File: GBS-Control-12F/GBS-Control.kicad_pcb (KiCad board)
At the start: 2 copper layers, 41.3 x 28.6 mm, 16 parts, among them J1 PROG, U1 PLCC-44 socket, U2 ESP-12F

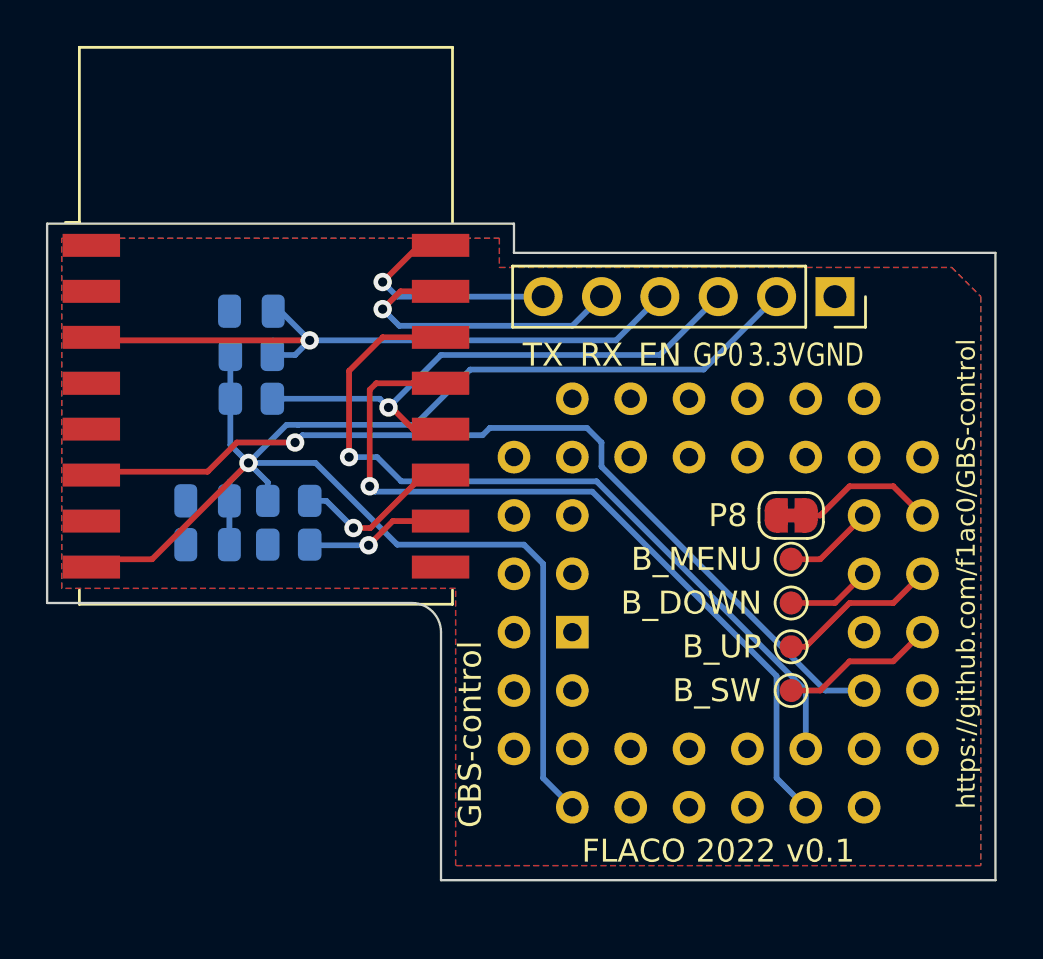
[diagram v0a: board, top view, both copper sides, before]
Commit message: KiCAD : add a port to connect the Si5351 Clock Generator
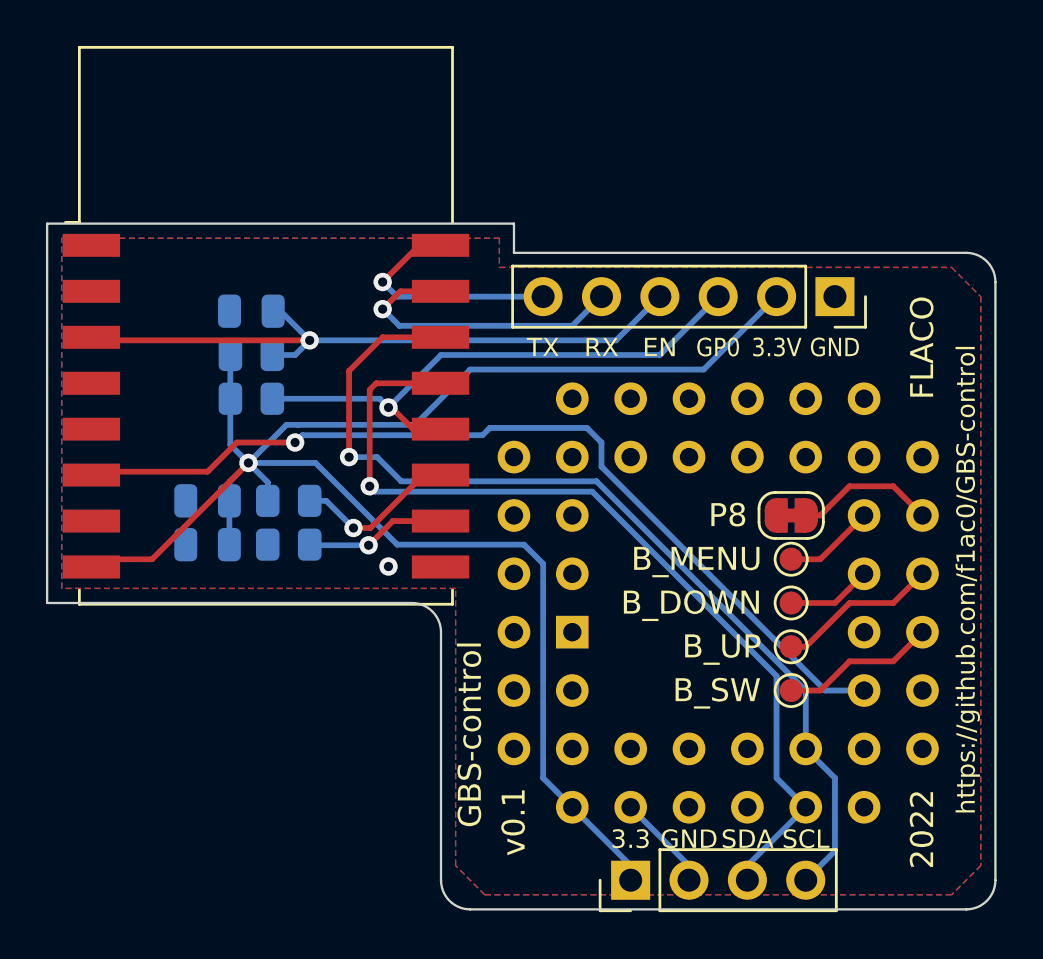
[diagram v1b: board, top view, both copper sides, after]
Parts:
- added J2: Clock port, Connector_PinHeader_2.54mm:PinHeader_1x04_P2.54mm_Vertical, F.Cu at (138.4, 102.9)
- TP1: value TestPoint -> B_UP
- TP2: value TestPoint -> B_DOWN
- TP3: value TestPoint -> B_SW
- TP4: value TestPoint -> B_MENU
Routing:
- net /SCL: track 35.0 -> 41.7 mm
- net /SDA: track 34.8 -> 39.0 mm
- net +3.3V: track 71.4 -> 75.6 mm
- net GND: track 0.00 -> 4.23 mm, vias 0 -> 1
- net /DISABLE: track 6.75 -> 6.12 mm
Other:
- board size 41.3 x 28.6 mm -> 41.3 x 29.8 mm
- board text added: "2022"
- board text added: "3.3"
- board text added: "FLACO"
- board text added: "SCL"
- board text added: "SDA"
- board text added: "v0.1"

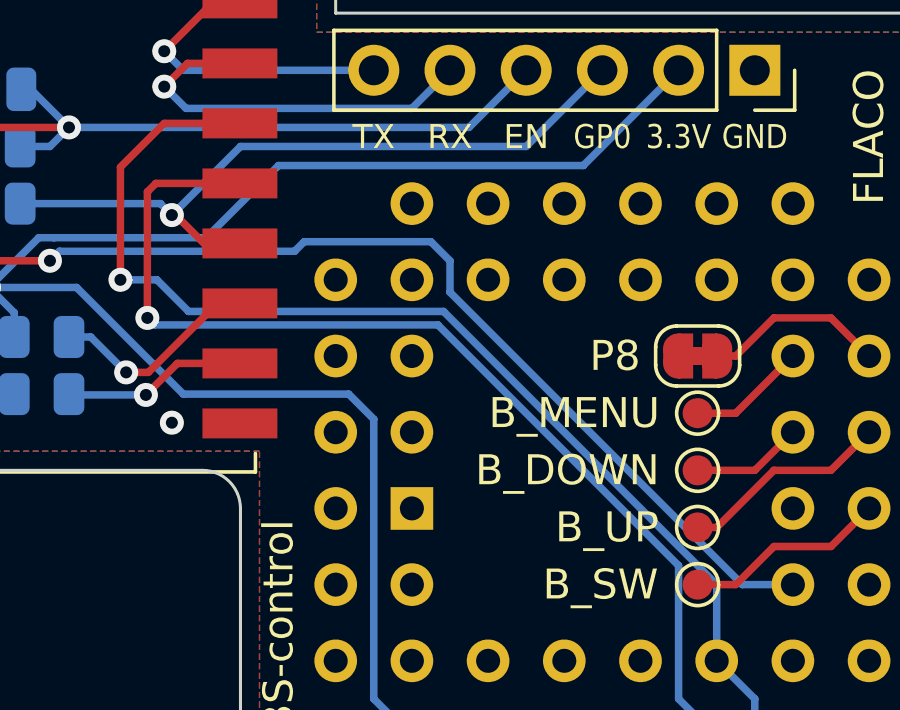
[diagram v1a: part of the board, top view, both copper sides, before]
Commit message: GBS-Control-12F, GBS-Control-M2 : update socket symbol and footprint, no PCB change
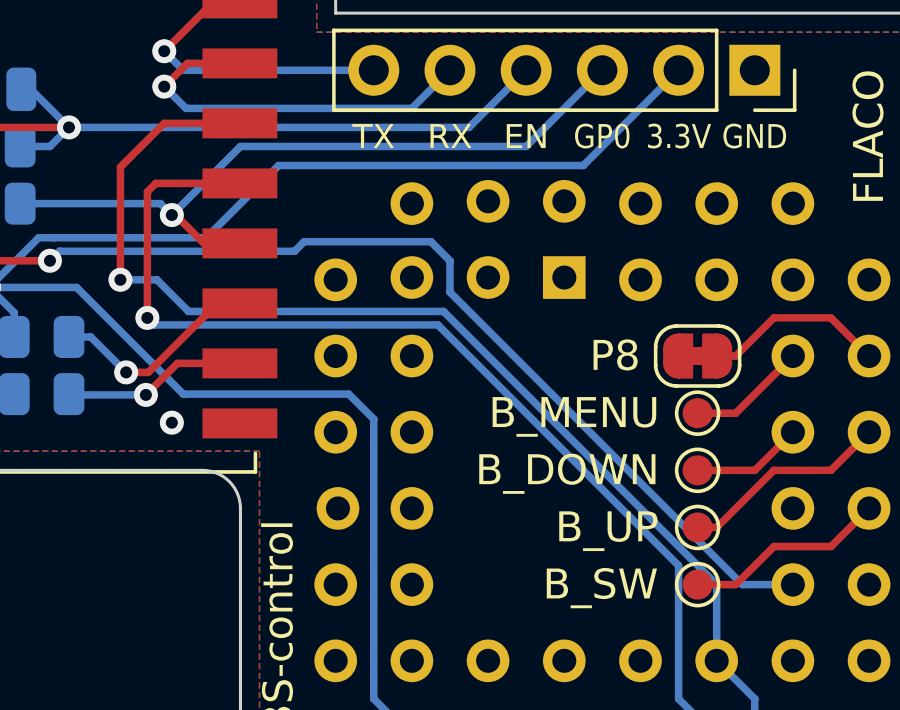
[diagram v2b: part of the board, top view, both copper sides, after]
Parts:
- U1: footprint Package_LCC:PLCC-44_THT-Socket -> Sassa:PLCC-44_THT-SocketOnTop
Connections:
- U1 pad 18: unconnected-(U1-Pad18) -> +3.3V
- U1 pad 20: /DISABLE -> GND
- U1 pad 21: /B_MENU -> unconnected-(U1-Pad21)
- U1 pad 22: /B_UP -> unconnected-(U1-Pad22)
- U1 pad 23: /B_DOWN -> unconnected-(U1-Pad23)
- U1 pad 24: /B_SW -> unconnected-(U1-Pad24)
- U1 pad 25: unconnected-(U1-Pad25) -> /SCL
- U1 pad 26: /RESET -> /SDA
- U1 pad 27: /DEBUG -> unconnected-(U1-Pad27)
- U1 pad 30: unconnected-(U1-Pad30) -> /DEBUG
- U1 pad 31: /SDA -> /RESET
- U1 pad 32: /SCL -> unconnected-(U1-Pad32)
- U1 pad 33: unconnected-(U1-Pad33) -> /B_SW
- U1 pad 34: unconnected-(U1-Pad34) -> /B_DOWN
- U1 pad 35: unconnected-(U1-Pad35) -> /B_UP
- U1 pad 36: unconnected-(U1-Pad36) -> /B_MENU
- U1 pad 37: GND -> /DISABLE
- U1 pad 39: +3.3V -> unconnected-(U1-Pad39)

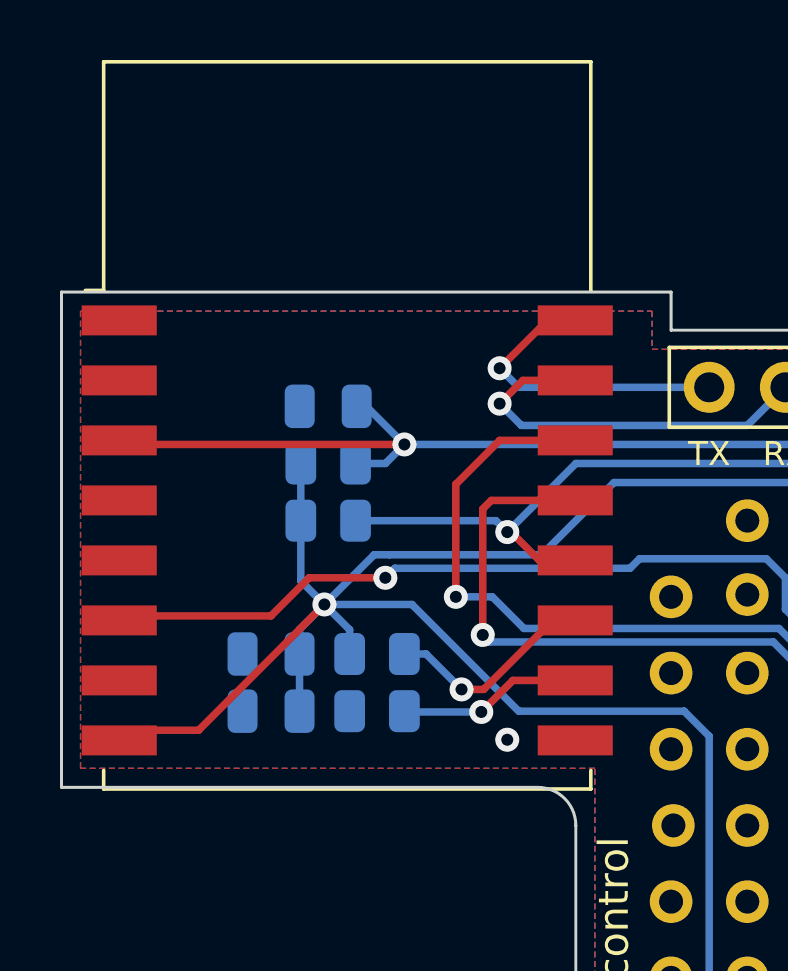
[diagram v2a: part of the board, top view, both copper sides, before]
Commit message: GBS-Control-12F, GBS-Control-M2 : update ibom ; small silkscreen change
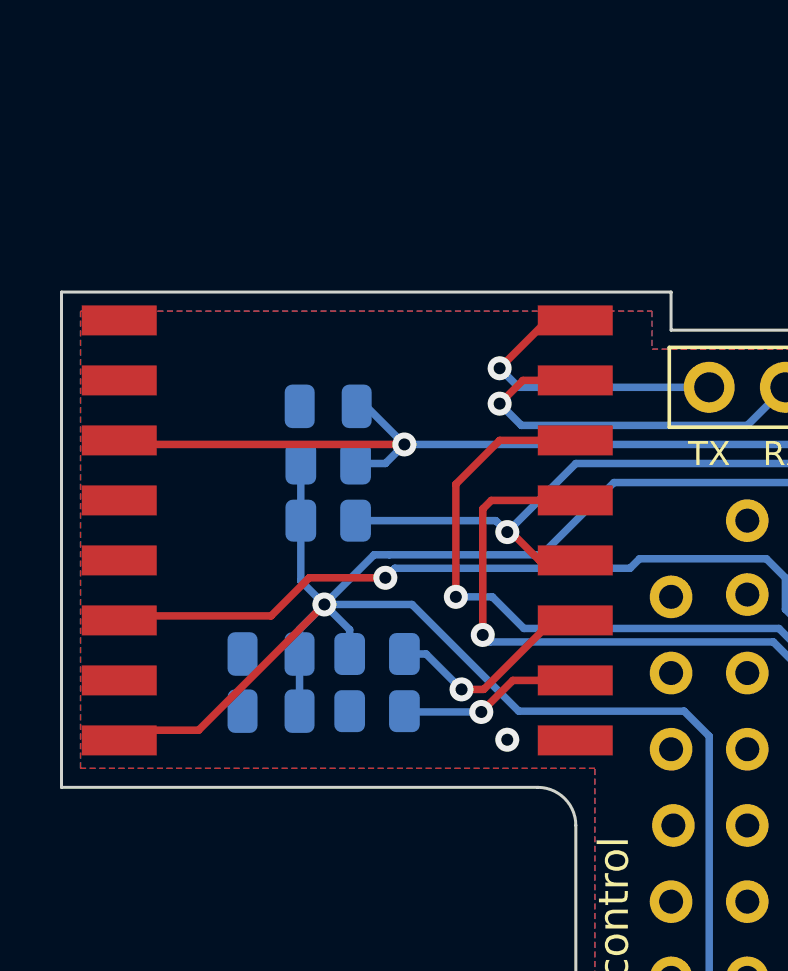
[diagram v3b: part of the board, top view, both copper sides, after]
